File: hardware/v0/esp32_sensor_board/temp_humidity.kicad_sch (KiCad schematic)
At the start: 2 parts, among them U601 SHT4x

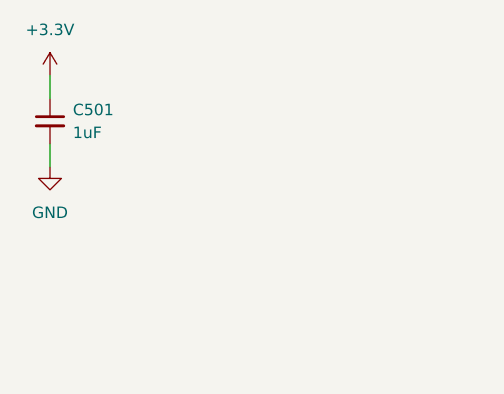
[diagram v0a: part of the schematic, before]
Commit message: INA237 progress, SHT4X comms working
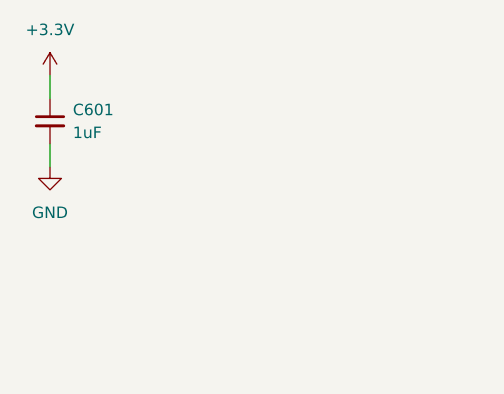
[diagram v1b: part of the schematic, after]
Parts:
- renumbered C501 to C601
